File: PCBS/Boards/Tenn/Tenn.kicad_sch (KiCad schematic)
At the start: 34 parts, among them J1 Conn_01x02_Socket, J10 Conn_01x03_Male, J11 Conn_01x03_Male, J12 Conn_01x04_Female, J13 Conn_01x03_Male, J14 Conn_01x03_Male, J15 Conn_01x03_Male, J16 Conn_01x02_Male, J17 Conn_01x02_Male, J2 Conn_01x03_Male, J3 Conn_01x03_Male, J4 Conn_01x03_Male, J5 Conn_01x03_Male, J6 Conn_01x03_Male, J7 Conn_01x03_Male, J8 Conn_01x03_Male, J9 Conn_01x03_Male, SW2 SW_Push, SW3 SW_Push, SW4 SW_SPDT, U1 L7805, U2 DRV8871DDA, U3 DRV8871DDA

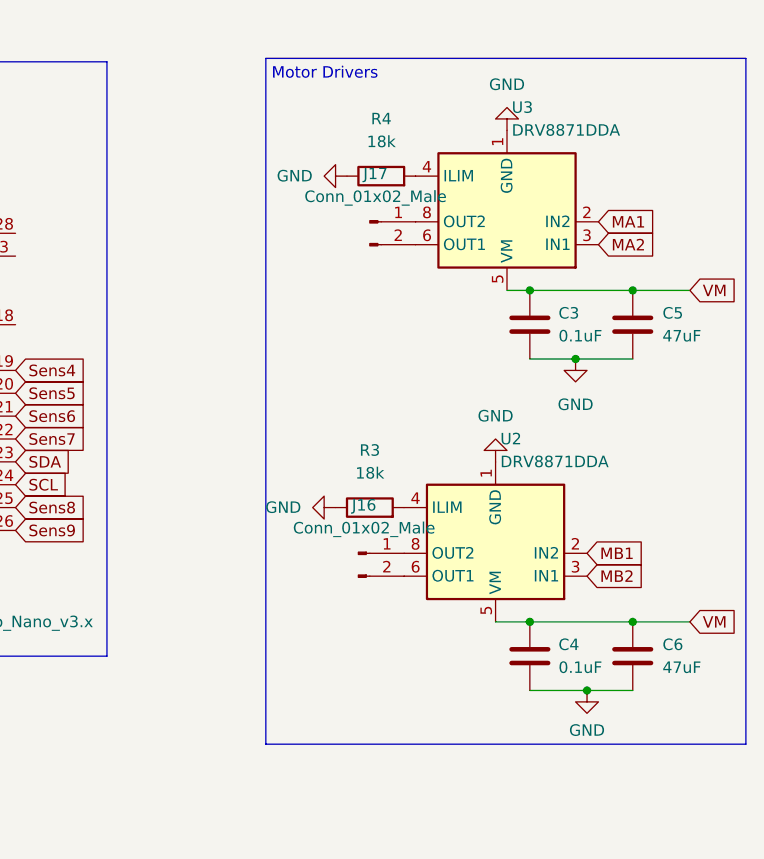
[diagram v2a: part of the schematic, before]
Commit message: updates tenn PCB board, changes some connections and netclasses
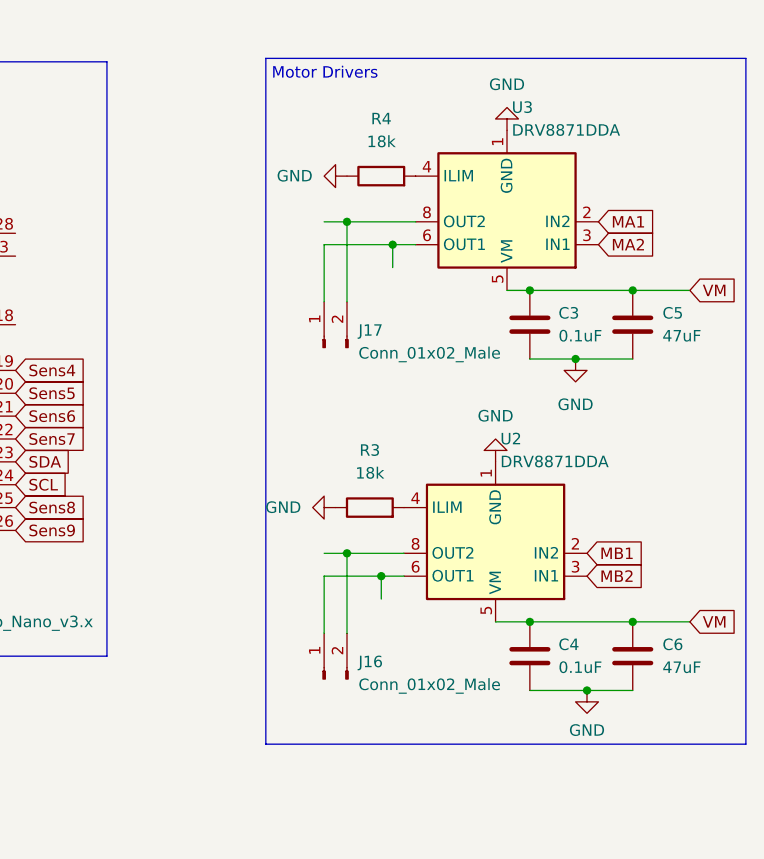
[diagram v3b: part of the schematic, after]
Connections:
- net at J16.1 (Pin_1): now also U2.6 (OUT1); no longer U2.8 (OUT2)
- net at J16.2 (Pin_2): now also U2.8 (OUT2); no longer U2.6 (OUT1)
- net at J17.1 (Pin_1): now also U3.6 (OUT1); no longer U3.8 (OUT2)
- net at J17.2 (Pin_2): now also U3.8 (OUT2); no longer U3.6 (OUT1)
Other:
- moved on the sheet: J16, J17
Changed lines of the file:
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@@
     (comment 2 "@tenn.bots")
   )
+  (junction (at 212.09 130.81) (diameter 0) (color 0 0 0 0)
+  )
   (junction (at 238.76 146.05) (diameter 0) (color 0 0 0 0)
   )
@@
   (junction (at 243.84 138.43) (diameter 0) (color 0 0 0 0)
   )
+  (junction (at 217.17 96.52) (diameter 0) (color 0 0 0 0)
+  )
   (junction (at 175.26 53.34) (diameter 0) (color 0 0 0 0)
   )
   (junction (at 232.41 101.6) (diameter 0) (color 0 0 0 0)
   )
+  (junction (at 215.9 133.35) (diameter 0) (color 0 0 0 0)
+  )
   (junction (at 103.632 48.26) (diameter 0) (color 0 0 0 0)
   )
@@
   )
   (junction (at 59.69 50.8) (diameter 0) (color 0 0 0 0)
+  )
+  (junction (at 212.09 93.98) (diameter 0) (color 0 0 0 0)
   )
   (junction (at 243.84 101.6) (diameter 0) (color 0 0 0 0)
@@
     (stroke (width 0) (type default))
   )
+  (wire (pts (xy 209.55 96.52) (xy 217.17 96.52))
+    (stroke (width 0) (type default))
+  )
   (polyline (pts (xy 88.9 114.3) (xy 121.92 114.3))
     (stroke (width 0) (type default))
   )
+  (wire (pts (xy 209.55 139.7) (xy 209.55 133.35))
+    (stroke (width 0) (type default))
+  )
   (polyline (pts (xy 203.073 75.819) (xy 256.413 75.819))
     (stroke (width 0) (type default))
@@
     (stroke (width 0) (type default))
   )
+  (wire (pts (xy 209.55 96.52) (xy 209.55 102.87))
+    (stroke (width 0) (type default))
+  )
+  (wire (pts (xy 217.17 96.52) (xy 219.71 96.52))
+    (stroke (width 0) (type default))
+  )
   (polyline (pts (xy 88.9 76.2) (xy 88.9 77.47))
     (stroke (width 0) (type default))
@@
     (stroke (width 0) (type default))
   )
+  (wire (pts (xy 209.55 93.98) (xy 212.09 93.98))
+    (stroke (width 0) (type default))
+  )
   (wire (pts (xy 100.838 48.26) (xy 103.632 48.26))
     (stroke (width 0) (type default))
@@
     (stroke (width 0) (type default))
   )
+  (wire (pts (xy 212.09 130.81) (xy 212.09 139.7))
+    (stroke (width 0) (type default))
+  )
   (polyline (pts (xy 127 38.1) (xy 127 60.96))
     (stroke (width 0) (type default))
@@
     (stroke (width 0) (type default))
   )
+  (wire (pts (xy 209.55 133.35) (xy 215.9 133.35))
+    (stroke (width 0) (type default))
+  )
   (polyline (pts (xy 114.3 95.25) (xy 114.3 76.2))
     (stroke (width 0) (type default))
   )
+  (wire (pts (xy 212.09 93.98) (xy 219.71 93.98))
+    (stroke (width 0) (type default))
+  )
   (wire (pts (xy 148.59 53.34) (xy 151.13 53.34))
     (stroke (width 0) (type default))
@@
     (stroke (width 0) (type default))
   )
+  (wire (pts (xy 212.09 93.98) (xy 212.09 102.87))
+    (stroke (width 0) (type default))
+  )
   (wire (pts (xy 59.69 50.8) (xy 64.77 50.8))
     (stroke (width 0) (type default))
@@
     (stroke (width 0) (type default))
   )
+  (wire (pts (xy 212.09 130.81) (xy 218.44 130.81))
+    (stroke (width 0) (type default))
+  )
   (polyline (pts (xy 203.073 152.019) (xy 256.413 152.019))
     (stroke (width 0) (type default))
@@
     (stroke (width 0) (type default))
   )
+  (wire (pts (xy 215.9 133.35) (xy 215.9 135.89))
+    (stroke (width 0) (type default))
+  )
   (polyline (pts (xy 114.3 76.2) (xy 88.9 76.2))
     (stroke (width 0) (type default))
   )
+  (wire (pts (xy 217.17 96.52) (xy 217.17 99.06))
+    (stroke (width 0) (type default))
+  )
   (wire (pts (xy 103.632 48.26) (xy 110.998 48.26))
     (stroke (width 0) (type default))
@@
   )
   (polyline (pts (xy 38.1 76.2) (xy 72.39 76.2))
+    (stroke (width 0) (type default))
+  )
+  (wire (pts (xy 209.55 130.81) (xy 212.09 130.81))
+    (stroke (width 0) (type default))
+  )
+  (wire (pts (xy 215.9 133.35) (xy 218.44 133.35))
     (stroke (width 0) (type default))
   )
@@
     )
   )
-  (netclass_flag "" (length 2.54) (shape round) (at 219.71 96.52 180) (fields_autoplaced)
+  (netclass_flag "" (length 2.54) (shape round) (at 217.17 99.06 180) (fields_autoplaced)
     (effects (font (size 1.27 1.27)) (justify right bottom))
-    (property "BatV" "" (at 220.4085 99.06 0) (show_name)
+    (property "Motor Out" "" (at 217.8685 101.6 0) (show_name)
       (effects (font (size 1.27 1.27) italic) (justify left))
     )
   )
-  (netclass_flag "" (length 2.54) (shape round) (at 219.71 93.98 0) (fields_autoplaced)
+  (netclass_flag "" (length 2.54) (shape round) (at 209.55 93.98 0) (fields_autoplaced)
     (effects (font (size 1.27 1.27)) (justify left bottom))
-    (property "BatV" "" (at 220.4085 91.44 0) (show_name)
+    (property "Motor Out" "" (at 210.2485 91.44 0) (show_name)
       (effects (font (size 1.27 1.27) italic) (justify left))
     )
   )
-  (netclass_flag "" (length 2.54) (shape round) (at 218.44 130.81 0) (fields_autoplaced)
+  (netclass_flag "" (length 2.54) (shape round) (at 209.55 130.81 0) (fields_autoplaced)
     (effects (font (size 1.27 1.27)) (justify left bottom))
-    (property "BatV" "" (at 219.1385 128.27 0) (show_name)
+    (property "Motor Out" "" (at 210.2485 128.27 0) (show_name)
       (effects (font (size 1.27 1.27) italic) (justify left))
     )
   )
-  (netclass_flag "" (length 2.54) (shape round) (at 218.44 133.35 180) (fields_autoplaced)
+  (netclass_flag "" (length 2.54) (shape round) (at 215.9 135.89 180) (fields_autoplaced)
     (effects (font (size 1.27 1.27)) (justify right bottom))
-    (property "BatV" "" (at 219.1385 135.89 0) (show_name)
+    (property "Motor Out" "" (at 216.5985 138.43 0) (show_name)
       (effects (font (size 1.27 1.27) italic) (justify left))
     )
@@
     )
   )
-  (symbol (lib_id "Connector:Conn_01x02_Male") (at 213.36 130.81 0) (unit 1)
-    (in_bom yes) (on_board yes) (dnp no) (fields_autoplaced)
-    (property "Reference" "J16" (at 213.995 125.476 0)
-      (effects (font (size 1.27 1.27)))
-    )
-    (property "Value" "Conn_01x02_Male" (at 213.995 128.016 0)
-      (effects (font (size 1.27 1.27)))
-    )
-    (property "Footprint" "Connector_JST:JST_XH_B2B-XH-A_1x02_P2.50mm_Vertical" (at 213.36 130.81 0)
-      (effects (font (size 1.27 1.27)) hide)
-    )
-    (property "Datasheet" "~" (at 213.36 130.81 0)
+  (symbol (lib_id "Connector:Conn_01x02_Male") (at 209.55 144.78 90) (unit 1)
+    (in_bom yes) (on_board yes) (dnp no) (fields_autoplaced)
+    (property "Reference" "J16" (at 213.36 142.875 90)
+      (effects (font (size 1.27 1.27)) (justify right))
+    )
+    (property "Value" "Conn_01x02_Male" (at 213.36 145.415 90)
+      (effects (font (size 1.27 1.27)) (justify right))
+    )
+    (property "Footprint" "Connector_JST:JST_XH_B2B-XH-A_1x02_P2.50mm_Vertical" (at 209.55 144.78 0)
+      (effects (font (size 1.27 1.27)) hide)
+    )
+    (property "Datasheet" "~" (at 209.55 144.78 0)
       (effects (font (size 1.27 1.27)) hide)
     )
@@
     )
   )
-  (symbol (lib_id "Connector:Conn_01x02_Male") (at 214.63 93.98 0) (unit 1)
-    (in_bom yes) (on_board yes) (dnp no) (fields_autoplaced)
-    (property "Reference" "J17" (at 215.265 88.646 0)
-      (effects (font (size 1.27 1.27)))
-    )
-    (property "Value" "Conn_01x02_Male" (at 215.265 91.186 0)
-      (effects (font (size 1.27 1.27)))
-    )
-    (property "Footprint" "Connector_JST:JST_XH_B2B-XH-A_1x02_P2.50mm_Vertical" (at 214.63 93.98 0)
-      (effects (font (size 1.27 1.27)) hide)
-    )
-    (property "Datasheet" "~" (at 214.63 93.98 0)
-      (effects (font (size 1.27 1.27)) hide)
-    )
+  (symbol (lib_id "Connector:Conn_01x02_Male") (at 209.55 107.95 90) (unit 1)
+    (in_bom yes) (on_board yes) (dnp no) (fields_autoplaced)
+    (property "Reference" "J17" (at 213.36 106.045 90)
+      (effects (font (size 1.27 1.27)) (justify right))
+    )
+    (property "Value" "Conn_01x02_Male" (at 213.36 108.585 90)
+      (effects (font (size 1.27 1.27)) (justify right))
+    )
+    (property "Footprint" "Connector_JST:JST_XH_B2B-XH-A_1x02_P2.50mm_Vertical" (at 209.55 107.95 0)
+      (effects (font (size 1.27 1.27)) hide)
+    )
+    (property "Datasheet" "~" (at 209.55 107.95 0)
+      (effects (font (size 1.27 1.27)) hide)
+    )

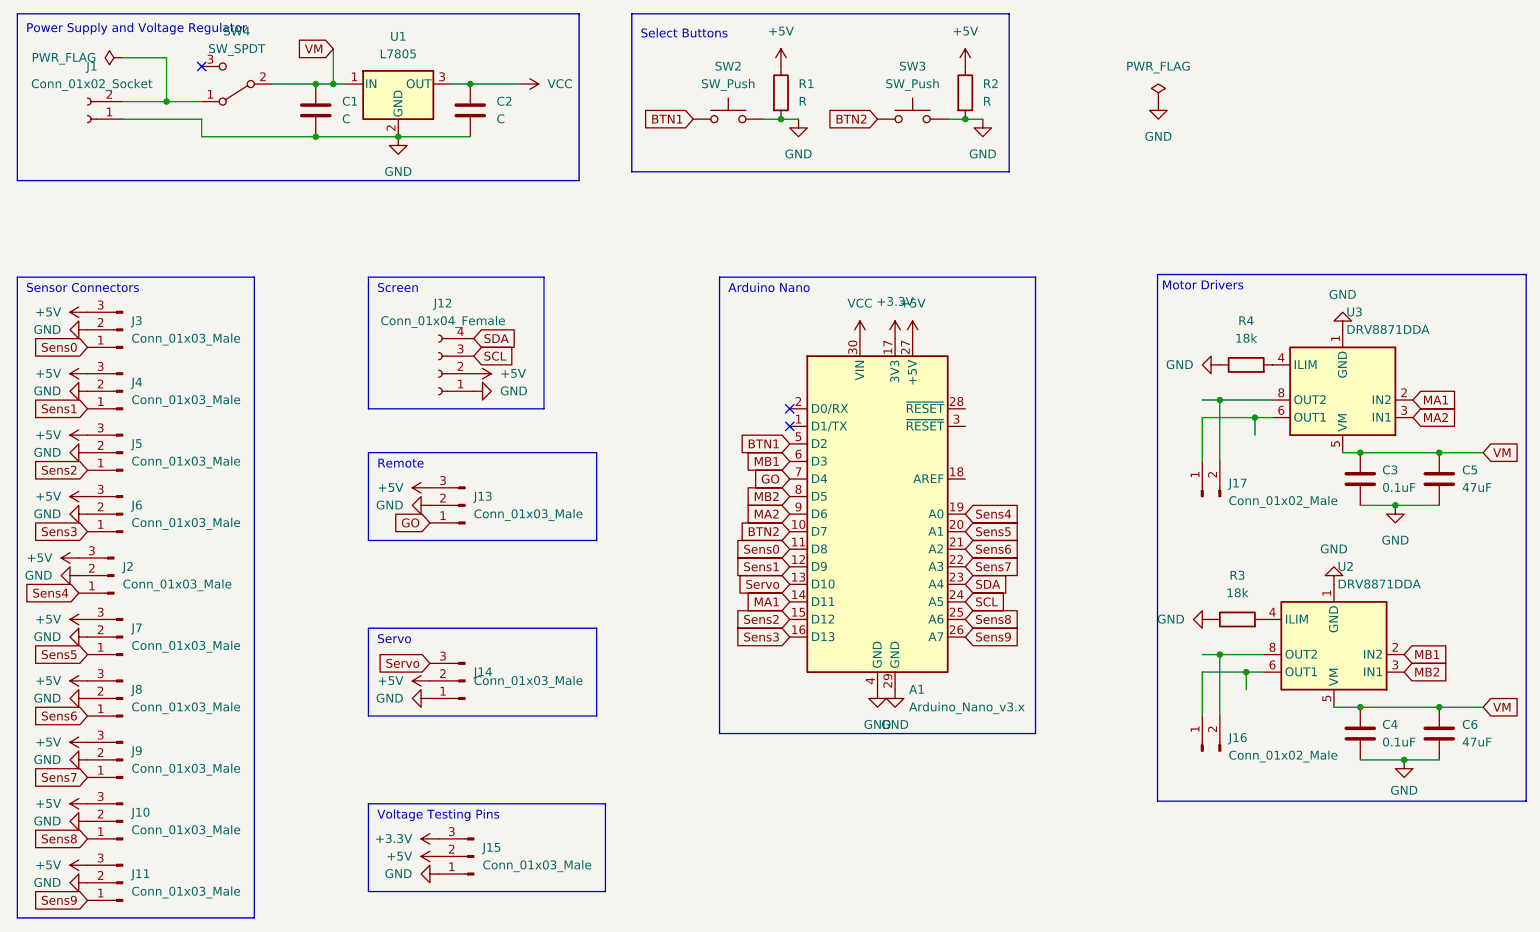
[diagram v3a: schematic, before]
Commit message: updates the files in Tenn PCB board
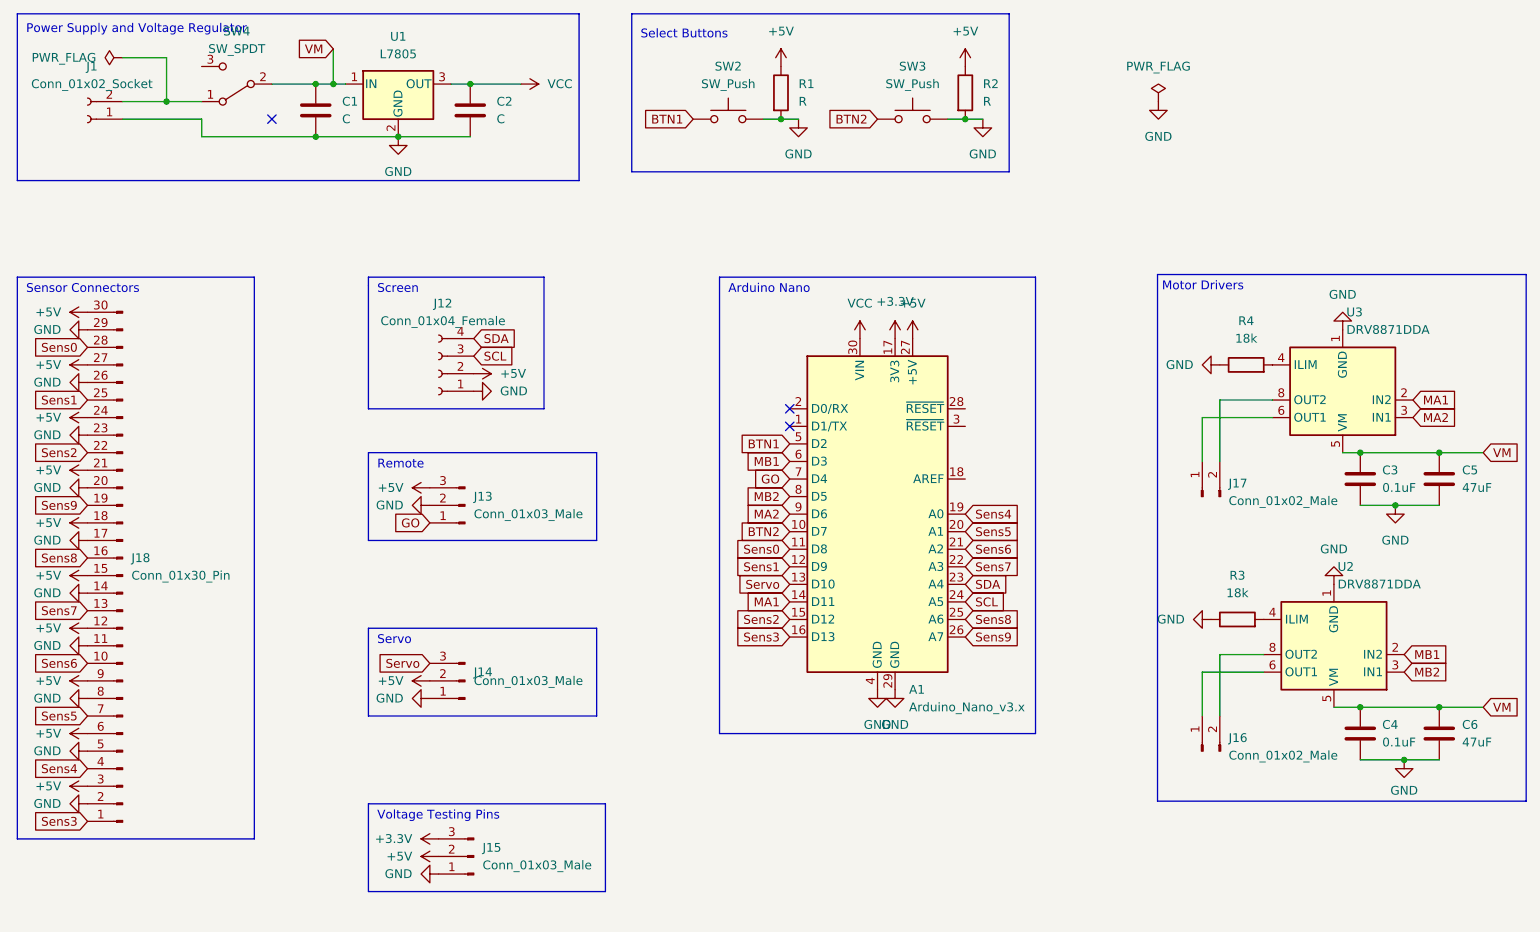
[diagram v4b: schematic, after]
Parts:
- removed J10, J11, J2, J3, J4, J5, J6, J7, J8, J9: Conn_01x03_Male, Connector_PinSocket_2.54mm:PinSocket_1x03_P2.54mm_Vertical, symbol Connector:Conn_01x03_Male
- added J18: Conn_01x30_Pin, Connector_PinSocket_2.54mm:PinSocket_1x30_P2.54mm_Vertical, symbol Connector:Conn_01x30_Pin
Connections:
- net +5V: now also J18.12 (Pin_12), J18.15 (Pin_15), J18.18 (Pin_18), J18.21 (Pin_21), J18.24 (Pin_24), J18.27 (Pin_27), J18.3 (Pin_3), J18.30 (Pin_30), J18.6 (Pin_6), J18.9 (Pin_9)
- net GND: now also J18.11 (Pin_11), J18.14 (Pin_14), J18.17 (Pin_17), J18.2 (Pin_2), J18.20 (Pin_20), J18.23 (Pin_23), J18.26 (Pin_26), J18.29 (Pin_29), J18.5 (Pin_5), J18.8 (Pin_8)
- net Sens0: now also J18.28 (Pin_28)
- net Sens1: now also J18.25 (Pin_25)
- net Sens2: now also J18.22 (Pin_22)
- net Sens3: now also J18.1 (Pin_1)
- net Sens4: now also J18.4 (Pin_4)
- net Sens5: now also J18.7 (Pin_7)
- net Sens6: now also J18.10 (Pin_10)
- net Sens7: now also J18.13 (Pin_13)
- net Sens8: now also J18.16 (Pin_16)
- net Sens9: now also J18.19 (Pin_19)
